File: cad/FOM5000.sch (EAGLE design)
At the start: 42 parts, among them Q1 DMN2300U-7, U1 MCP7941X, U2 AT30TS75A-SS, U3 MCP3424-E/SL, U4 MCP1824T-ADJE/OT, Y1 32.768KHz

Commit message: Add pullup resistor on RTCMFP
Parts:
- added R11: 10K 5%, C3-Panasonic:ERJ-3GEYJ103
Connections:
- net RTCMFC: now also R11.1
- net VCC: now also R11.2
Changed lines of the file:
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@@
 <part name="SJ2" library="C3-General" deviceset="SOLDERJUMPER_2WAY" device="PASTE2&amp;3"/>
 <part name="SJ3" library="C3-General" deviceset="SOLDERJUMPER_2WAY" device="PASTE2&amp;3"/>
+<part name="U$27" library="C3-General" deviceset="VCC" device=""/>
+<part name="R11" library="C3-Panasonic" deviceset="ERJ-?*" device="3GEY" technology="J103" value="10K 5%"/>
 </parts>
 <sheets>
@@
 <instance part="SJ2" gate="A" x="251.46" y="220.98"/>
 <instance part="SJ3" gate="A" x="236.22" y="215.9"/>
+<instance part="U$27" gate="G$1" x="147.32" y="68.58"/>
+<instance part="R11" gate="A" x="147.32" y="55.88" rot="R90"/>
 </instances>
 <busses>
@@
 <wire x1="317.5" y1="129.54" x2="320.04" y2="129.54" width="0.1524" layer="91"/>
 </segment>
+<segment>
+<pinref part="U$27" gate="G$1" pin="VCC"/>
+<pinref part="R11" gate="A" pin="2"/>
+<wire x1="147.32" y1="68.58" x2="147.32" y2="66.04" width="0.1524" layer="91"/>
+</segment>
 </net>
 <net name="VIN" class="0">
@@
 <segment>
 <wire x1="266.7" y1="111.76" x2="266.7" y2="53.34" width="0.1524" layer="91"/>
-<wire x1="266.7" y1="53.34" x2="167.64" y2="53.34" width="0.1524" layer="91"/>
-<wire x1="167.64" y1="53.34" x2="167.64" y2="71.12" width="0.1524" layer="91"/>
+<wire x1="266.7" y1="53.34" x2="147.32" y2="53.34" width="0.1524" layer="91"/>
+<wire x1="147.32" y1="53.34" x2="137.16" y2="53.34" width="0.1524" layer="91"/>
+<wire x1="137.16" y1="53.34" x2="137.16" y2="71.12" width="0.1524" layer="91"/>
 <pinref part="U1" gate="A" pin="MFP"/>
-<wire x1="167.64" y1="71.12" x2="127" y2="71.12" width="0.1524" layer="91"/>
+<wire x1="137.16" y1="71.12" x2="127" y2="71.12" width="0.1524" layer="91"/>
 <label x="259.588" y="112.268" size="1.27" layer="95" font="vector"/>
 <pinref part="PI" gate="A" pin="GPIO25"/>
 <wire x1="266.7" y1="111.76" x2="259.08" y2="111.76" width="0.1524" layer="91"/>
-</segment>
-</net>
+<pinref part="R11" gate="A" pin="1"/>
+<wire x1="147.32" y1="55.88" x2="147.32" y2="53.34" width="0.1524" layer="91"/>
+<junction x="147.32" y="53.34"/>
+</segment>
+</net>

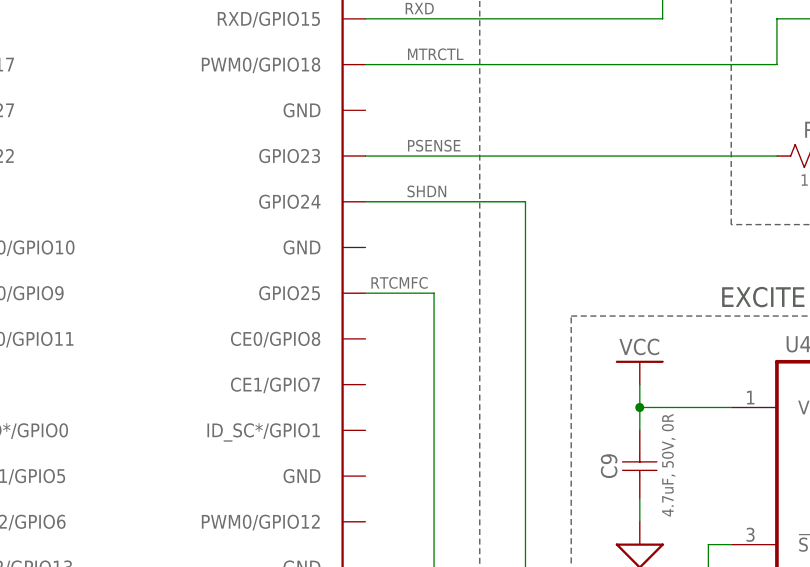
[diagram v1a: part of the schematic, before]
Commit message: Rename mislabeled net RTCMFP
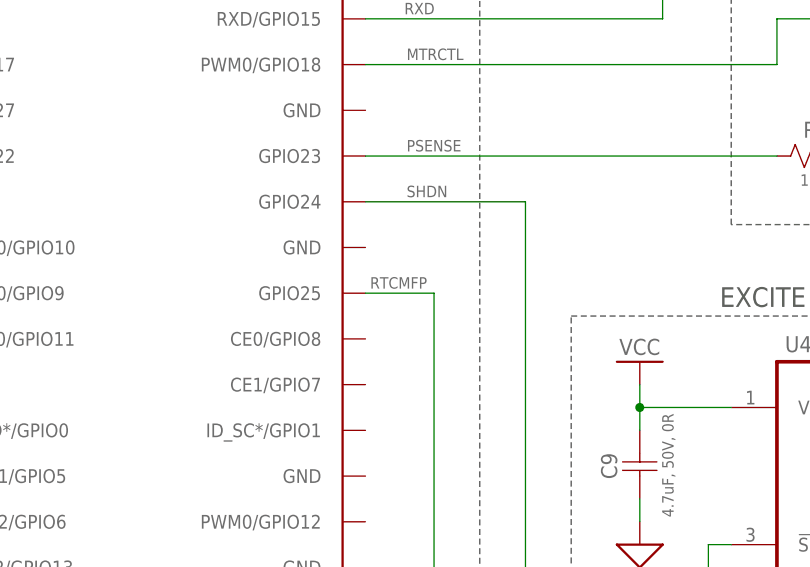
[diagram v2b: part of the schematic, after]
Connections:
- net RTCMFC renamed RTCMFP
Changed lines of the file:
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@@
 </segment>
 </net>
-<net name="RTCMFC" class="0">
+<net name="RTCMFP" class="0">
 <segment>
 <wire x1="266.7" y1="111.76" x2="266.7" y2="53.34" width="0.1524" layer="91"/>

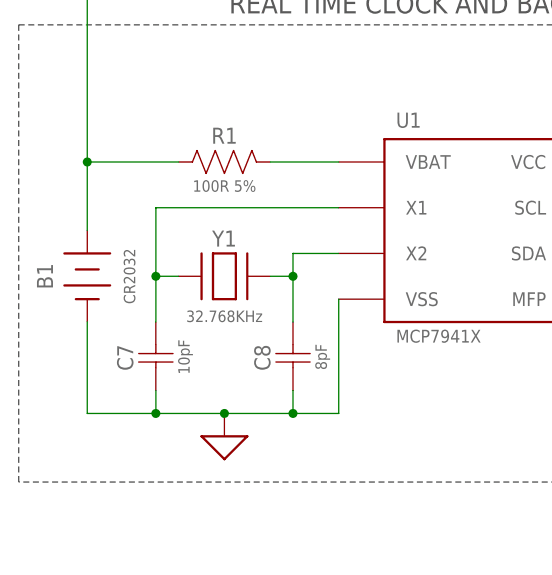
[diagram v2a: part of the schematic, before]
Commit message: Add schottky diode on VBAT for UL compliance; change VBAT load limiting resistor to 1K per AN-1365
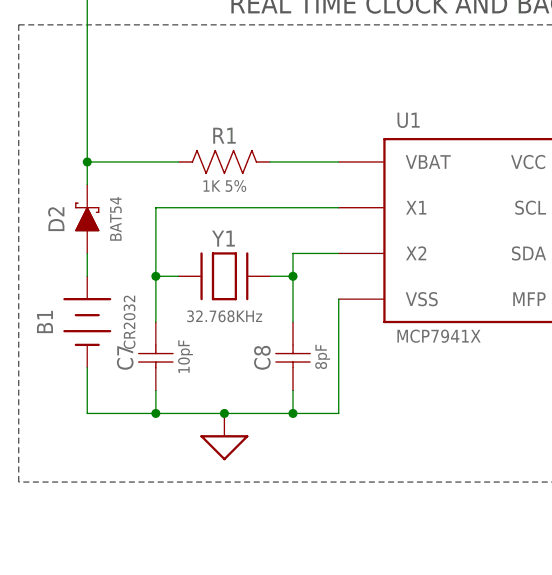
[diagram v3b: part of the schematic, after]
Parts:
- added D2: BAT54, C3-RCL:BAT54
- R1: value 100R 5% -> 1K 5%; device C3-Panasonic:ERJ-3GEYJ101 -> C3-Panasonic:ERJ-3GEYJ102
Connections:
- new net N$2: D2.C, R1.1, R4.1
- net VBAT: now also D2.A; no longer R1.1, R4.1
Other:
- moved on the sheet: B1
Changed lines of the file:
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@@
 <part name="C6" library="C3-Murata" deviceset="GRM18*" device="" technology="8R71E104KA01" value="0.1uF"/>
 <part name="B1" library="C3-Battery" deviceset="BU2032SM-HD-G" device="" value="CR2032"/>
-<part name="R1" library="C3-Panasonic" deviceset="ERJ-?*" device="3GEY" technology="J101" value="100R 5%"/>
+<part name="R1" library="C3-Panasonic" deviceset="ERJ-?*" device="3GEY" technology="J102" value="1K 5%"/>
 <part name="U$5" library="C3-General" deviceset="GND" device=""/>
 <part name="U$6" library="C3-General" deviceset="GND" device=""/>
@@
 <part name="U$27" library="C3-General" deviceset="VCC" device=""/>
 <part name="R11" library="C3-Panasonic" deviceset="ERJ-?*" device="3GEY" technology="J103" value="10K 5%"/>
+<part name="D2" library="C3-RCL" deviceset="BAT54" device=""/>
 </parts>
 <sheets>
@@
 <instance part="C5" gate="A" x="114.3" y="228.6" rot="R90"/>
 <instance part="C6" gate="A" x="88.9" y="228.6" rot="R90"/>
-<instance part="B1" gate="A" x="68.58" y="73.66" rot="MR270"/>
+<instance part="B1" gate="A" x="68.58" y="68.58" rot="MR270"/>
 <instance part="R1" gate="A" x="78.74" y="86.36"/>
 <instance part="U$5" gate="1" x="76.2" y="134.62"/>
@@
 <instance part="U$27" gate="G$1" x="147.32" y="68.58"/>
 <instance part="R11" gate="A" x="147.32" y="55.88" rot="R90"/>
+<instance part="D2" gate="G$1" x="68.58" y="81.28" rot="R90"/>
 </instances>
 <busses>
@@
 <wire x1="76.2" y1="58.42" x2="83.82" y2="58.42" width="0.1524" layer="91"/>
 <junction x="83.82" y="58.42"/>
-<wire x1="68.58" y1="68.58" x2="68.58" y2="58.42" width="0.1524" layer="91"/>
+<wire x1="68.58" y1="63.5" x2="68.58" y2="58.42" width="0.1524" layer="91"/>
 <wire x1="68.58" y1="58.42" x2="76.2" y2="58.42" width="0.1524" layer="91"/>
 <junction x="76.2" y="58.42"/>
@@
 <segment>
 <pinref part="B1" gate="A" pin="VBAT"/>
-<pinref part="R1" gate="A" pin="1"/>
-<wire x1="68.58" y1="78.74" x2="68.58" y2="86.36" width="0.1524" layer="91"/>
-<wire x1="68.58" y1="86.36" x2="78.74" y2="86.36" width="0.1524" layer="91"/>
-<wire x1="68.58" y1="121.92" x2="68.58" y2="86.36" width="0.1524" layer="91"/>
-<junction x="68.58" y="86.36"/>
-<pinref part="R4" gate="A" pin="1"/>
+<pinref part="D2" gate="G$1" pin="A"/>
+<wire x1="68.58" y1="73.66" x2="68.58" y2="76.2" width="0.1524" layer="91"/>
 </segment>
 </net>
@@
 </segment>
 </net>
+<net name="N$2" class="0">
+<segment>
+<pinref part="R1" gate="A" pin="1"/>
+<wire x1="68.58" y1="83.82" x2="68.58" y2="86.36" width="0.1524" layer="91"/>
+<wire x1="68.58" y1="86.36" x2="78.74" y2="86.36" width="0.1524" layer="91"/>
+<wire x1="68.58" y1="121.92" x2="68.58" y2="86.36" width="0.1524" layer="91"/>
+<junction x="68.58" y="86.36"/>
+<pinref part="R4" gate="A" pin="1"/>
+<pinref part="D2" gate="G$1" pin="C"/>
+</segment>
+</net>

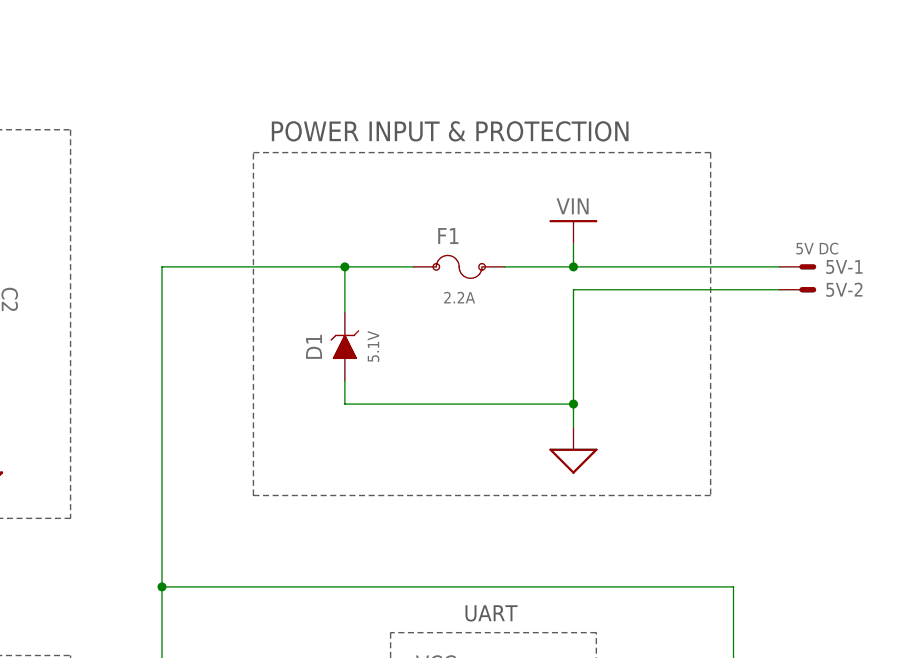
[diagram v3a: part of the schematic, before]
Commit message: Added some input capacitance
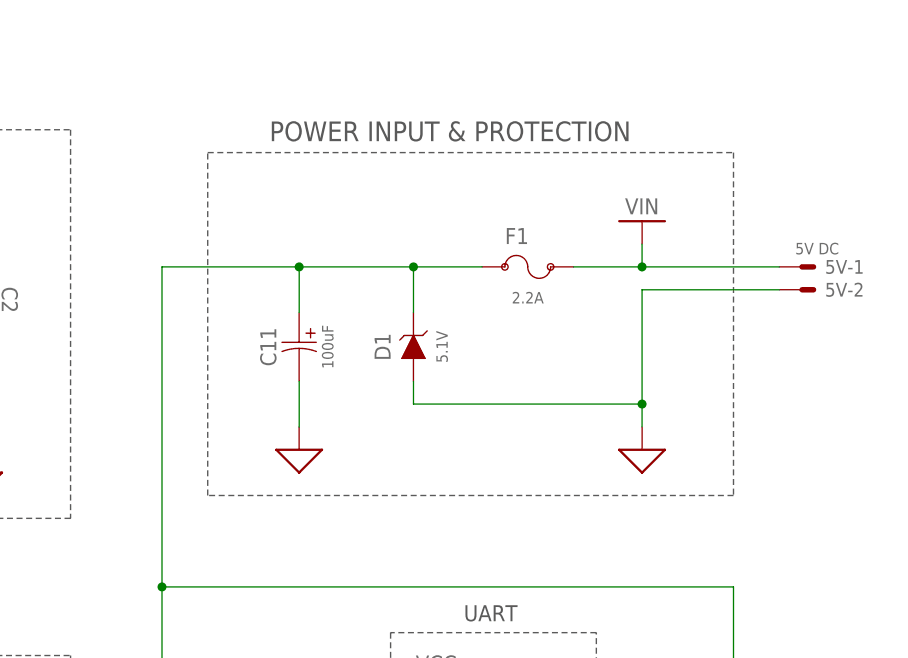
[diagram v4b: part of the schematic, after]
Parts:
- added C11: 100uF, C3-Nichicon:UWT0G102MNL1GS/8
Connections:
- net 5V: now also C11.POS
- net GND: now also C11.NEG
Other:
- moved on the sheet: D1, F1
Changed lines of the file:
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@@
 <part name="R11" library="C3-Panasonic" deviceset="ERJ-?*" device="3GEY" technology="J103" value="10K 5%"/>
 <part name="D2" library="C3-RCL" deviceset="BAT54" device=""/>
+<part name="C11" library="C3-Nichicon" deviceset="UWT*M?" device="NL1GS/8" technology="0G102" value="100uF"/>
+<part name="U$29" library="C3-General" deviceset="GND" device=""/>
 </parts>
 <sheets>
@@
 <wire x1="299.72" y1="119.38" x2="299.72" y2="152.4" width="0.1524" layer="97" style="shortdash"/>
 <text x="318.262" y="153.67" size="2.1844" layer="97" font="vector" ratio="16">MOTOR CONTROL</text>
-<wire x1="342.9" y1="205.74" x2="292.1" y2="205.74" width="0.1524" layer="97" style="shortdash"/>
-<wire x1="292.1" y1="205.74" x2="292.1" y2="243.84" width="0.1524" layer="97" style="shortdash"/>
-<wire x1="292.1" y1="243.84" x2="342.9" y2="243.84" width="0.1524" layer="97" style="shortdash"/>
-<wire x1="342.9" y1="243.84" x2="342.9" y2="205.74" width="0.1524" layer="97" style="shortdash"/>
+<wire x1="345.44" y1="205.74" x2="287.02" y2="205.74" width="0.1524" layer="97" style="shortdash"/>
+<wire x1="287.02" y1="205.74" x2="287.02" y2="243.84" width="0.1524" layer="97" style="shortdash"/>
+<wire x1="287.02" y1="243.84" x2="345.44" y2="243.84" width="0.1524" layer="97" style="shortdash"/>
+<wire x1="345.44" y1="243.84" x2="345.44" y2="205.74" width="0.1524" layer="97" style="shortdash"/>
 <text x="293.878" y="245.11" size="2.1844" layer="97" font="vector" ratio="16">POWER INPUT &amp; PROTECTION</text>
 <wire x1="137.16" y1="254" x2="137.16" y2="180.34" width="0.1524" layer="97" style="shortdash"/>
@@
 <instance part="5V" gate="-1" x="353.06" y="231.14"/>
 <instance part="5V" gate="-2" x="353.06" y="228.6"/>
-<instance part="F1" gate="A" x="314.96" y="231.14"/>
+<instance part="F1" gate="A" x="322.58" y="231.14"/>
 <instance part="LC1" gate="1" x="83.82" y="238.76" rot="R180"/>
 <instance part="LC1" gate="2" x="88.9" y="137.16" rot="R180"/>
@@
 <instance part="R3" gate="A" x="187.96" y="162.56" rot="R90"/>
 <instance part="U$9" gate="G$1" x="195.58" y="177.8"/>
-<instance part="D1" gate="A" x="302.26" y="218.44" rot="R90"/>
-<instance part="U$11" gate="1" x="327.66" y="213.36"/>
+<instance part="D1" gate="A" x="309.88" y="218.44" rot="R90"/>
+<instance part="U$11" gate="1" x="335.28" y="213.36"/>
 <instance part="U$12" gate="A" x="114.3" y="241.3"/>
 <instance part="U$13" gate="G$1" x="127" y="93.98"/>
 <instance part="VCC" gate="G$1" x="289.56" y="101.6"/>
-<instance part="U$10" gate="A" x="327.66" y="236.22"/>
+<instance part="U$10" gate="A" x="335.28" y="236.22"/>
 <instance part="Y1" gate="A" x="83.82" y="73.66"/>
 <instance part="C7" gate="A" x="76.2" y="60.96" rot="R90"/>
@@
 <instance part="R11" gate="A" x="147.32" y="55.88" rot="R90"/>
 <instance part="D2" gate="G$1" x="68.58" y="81.28" rot="R90"/>
+<instance part="C11" gate="A" x="297.18" y="220.98" rot="R90"/>
+<instance part="U$29" gate="1" x="297.18" y="213.36"/>
 </instances>
 <busses>
@@
 <segment>
 <pinref part="U$11" gate="1" pin="GND"/>
-<wire x1="327.66" y1="213.36" x2="327.66" y2="215.9" width="0.1524" layer="91"/>
-<wire x1="327.66" y1="215.9" x2="327.66" y2="228.6" width="0.1524" layer="91"/>
+<wire x1="335.28" y1="213.36" x2="335.28" y2="215.9" width="0.1524" layer="91"/>
+<wire x1="335.28" y1="215.9" x2="335.28" y2="228.6" width="0.1524" layer="91"/>
 <pinref part="D1" gate="A" pin="A"/>
-<wire x1="302.26" y1="218.44" x2="302.26" y2="215.9" width="0.1524" layer="91"/>
-<wire x1="302.26" y1="215.9" x2="327.66" y2="215.9" width="0.1524" layer="91"/>
-<junction x="327.66" y="215.9"/>
+<wire x1="309.88" y1="218.44" x2="309.88" y2="215.9" width="0.1524" layer="91"/>
+<wire x1="309.88" y1="215.9" x2="335.28" y2="215.9" width="0.1524" layer="91"/>
+<junction x="335.28" y="215.9"/>
 <pinref part="5V" gate="-2" pin="S"/>
-<wire x1="327.66" y1="228.6" x2="350.52" y2="228.6" width="0.1524" layer="91"/>
+<wire x1="335.28" y1="228.6" x2="350.52" y2="228.6" width="0.1524" layer="91"/>
 </segment>
 <segment>
@@
 <wire x1="261.62" y1="223.52" x2="261.62" y2="218.44" width="0.1524" layer="91"/>
 <junction x="261.62" y="218.44"/>
+</segment>
+<segment>
+<pinref part="C11" gate="A" pin="NEG"/>
+<pinref part="U$29" gate="1" pin="GND"/>
+<wire x1="297.18" y1="218.44" x2="297.18" y2="213.36" width="0.1524" layer="91"/>
 </segment>
 </net>
@@
 <net name="VIN" class="0">
 <segment>
-<wire x1="327.66" y1="231.14" x2="327.66" y2="233.68" width="0.1524" layer="91"/>
+<wire x1="335.28" y1="231.14" x2="335.28" y2="233.68" width="0.1524" layer="91"/>
 <pinref part="U$10" gate="A" pin="VIN"/>
 <pinref part="5V" gate="-1" pin="S"/>
-<wire x1="350.52" y1="231.14" x2="327.66" y2="231.14" width="0.1524" layer="91"/>
+<wire x1="350.52" y1="231.14" x2="335.28" y2="231.14" width="0.1524" layer="91"/>
 <pinref part="F1" gate="A" pin="2"/>
-<wire x1="320.04" y1="231.14" x2="327.66" y2="231.14" width="0.1524" layer="91"/>
-<junction x="327.66" y="231.14"/>
+<wire x1="327.66" y1="231.14" x2="335.28" y2="231.14" width="0.1524" layer="91"/>
+<junction x="335.28" y="231.14"/>
 </segment>
 </net>
@@
 <segment>
 <pinref part="D1" gate="A" pin="C"/>
-<wire x1="302.26" y1="231.14" x2="302.26" y2="226.06" width="0.1524" layer="91"/>
+<wire x1="309.88" y1="231.14" x2="309.88" y2="226.06" width="0.1524" layer="91"/>
 <wire x1="259.08" y1="162.56" x2="281.94" y2="162.56" width="0.1524" layer="91"/>
 <wire x1="281.94" y1="162.56" x2="281.94" y2="195.58" width="0.1524" layer="91"/>
 <wire x1="281.94" y1="195.58" x2="281.94" y2="231.14" width="0.1524" layer="91"/>
-<wire x1="281.94" y1="231.14" x2="302.26" y2="231.14" width="0.1524" layer="91"/>
+<wire x1="281.94" y1="231.14" x2="297.18" y2="231.14" width="0.1524" layer="91"/>
 <pinref part="Q1" gate="A" pin="D"/>
+<wire x1="297.18" y1="231.14" x2="309.88" y2="231.14" width="0.1524" layer="91"/>
 <wire x1="345.44" y1="147.32" x2="345.44" y2="195.58" width="0.1524" layer="91"/>
 <wire x1="345.44" y1="195.58" x2="281.94" y2="195.58" width="0.1524" layer="91"/>
@@
 <junction x="281.94" y="162.56"/>
 <pinref part="F1" gate="A" pin="1"/>
-<wire x1="309.88" y1="231.14" x2="302.26" y2="231.14" width="0.1524" layer="91"/>
-<junction x="302.26" y="231.14"/>
+<wire x1="317.5" y1="231.14" x2="309.88" y2="231.14" width="0.1524" layer="91"/>
+<junction x="309.88" y="231.14"/>
 <pinref part="PI" gate="A" pin="5V@2"/>
 <pinref part="PI" gate="A" pin="5V@4"/>
-</segment>
-</net>
+<pinref part="C11" gate="A" pin="POS"/>
+<wire x1="297.18" y1="226.06" x2="297.18" y2="231.14" width="0.1524" layer="91"/>
+<junction x="297.18" y="231.14"/>
+</segment>
+</net>

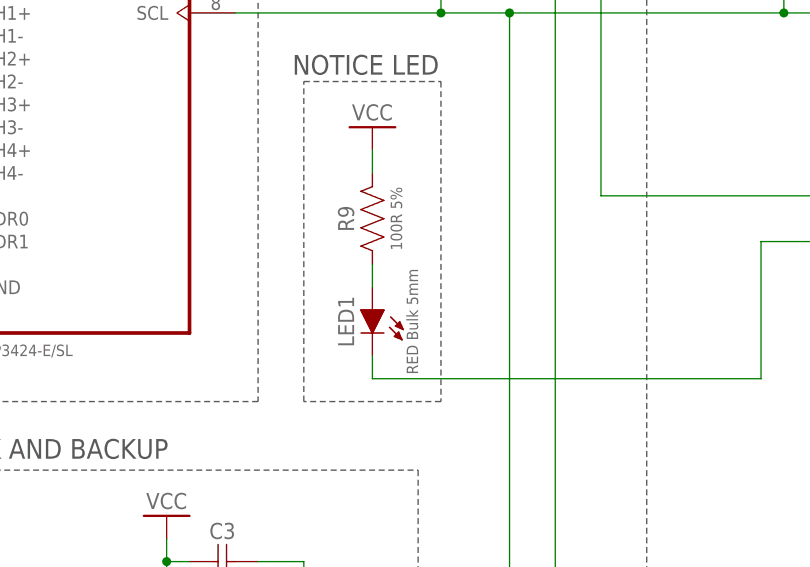
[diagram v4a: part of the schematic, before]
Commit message: Change R9 to 330R
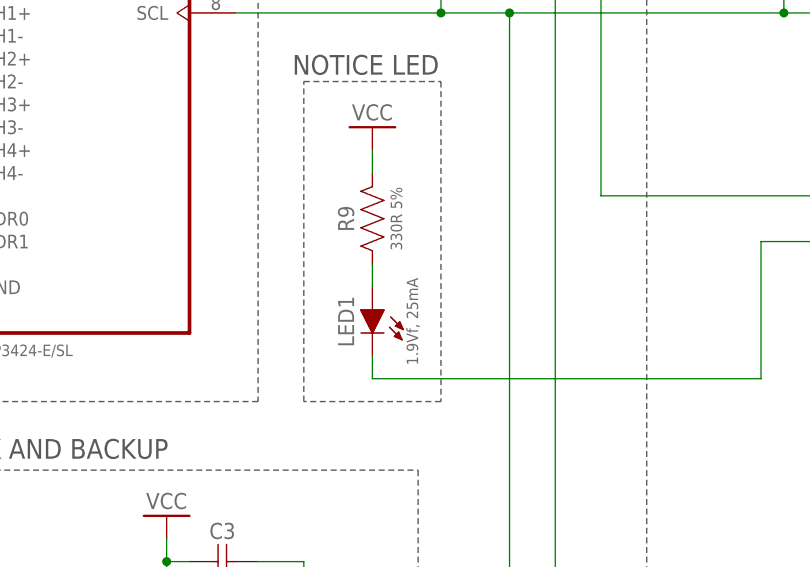
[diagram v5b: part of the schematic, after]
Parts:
- LED1: value RED Bulk 5mm -> 1.9Vf, 25mA
- R9: value 100R 5% -> 330R 5%; device C3-Panasonic:ERJ-3GEYJ101 -> C3-Panasonic:ERJ-3GEYJ331
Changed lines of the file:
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@@
 <part name="U$2" library="C3-General" deviceset="+2V4" device=""/>
 <part name="FRAME1" library="C3-General" deviceset="FRAME_B_L" device="" value="FOM5000"/>
-<part name="LED1" library="C3-LED" deviceset="LED" device="5MM" value="RED Bulk 5mm"/>
-<part name="R9" library="C3-Panasonic" deviceset="ERJ-?*" device="3GEY" technology="J101" value="100R 5%"/>
+<part name="LED1" library="C3-LED" deviceset="LED" device="5MM" value="1.9Vf, 25mA"/>
+<part name="R9" library="C3-Panasonic" deviceset="ERJ-?*" device="3GEY" technology="J331" value="330R 5%"/>
 <part name="U$14" library="C3-General" deviceset="VCC" device=""/>
 <part name="U$18" library="C3-General" deviceset="GND" device=""/>
